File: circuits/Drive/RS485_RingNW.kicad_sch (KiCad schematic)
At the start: 30 parts, among them J13 Conn_01x06_MountingPin, J8 Conn_01x06_MountingPin, Q17 S8550, Q5 S8550, U11 MAX3485, U12 MAX3485, U14 MAX3485, U16 MAX3485

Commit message: 更新
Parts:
- J13, J8: footprint Connector_Molex:Molex_PicoBlade_53261-0671_1x06-1MP_P1.25mm_Horizontal -> Connector_Molex:Molex_PicoBlade_53398-0671_1x06-1MP_P1.25mm_Vertical
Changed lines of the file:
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@@
       (effects (font (size 1.27 1.27)) (justify left))
     )
-    (property "Footprint" "Connector_Molex:Molex_PicoBlade_53261-0671_1x06-1MP_P1.25mm_Horizontal" (at 142.24 86.36 0)
+    (property "Footprint" "Connector_Molex:Molex_PicoBlade_53398-0671_1x06-1MP_P1.25mm_Vertical" (at 142.24 86.36 0)
       (effects (font (size 1.27 1.27)) hide)
     )
@@
       (effects (font (size 1.27 1.27)) (justify left))
     )
-    (property "Footprint" "Connector_Molex:Molex_PicoBlade_53261-0671_1x06-1MP_P1.25mm_Horizontal" (at 276.86 86.36 0)
-      (effects (font (size 1.27 1.27)) hide)
-    )
+    (property "Footprint" "Connector_Molex:Molex_PicoBlade_53398-0671_1x06-1MP_P1.25mm_Vertical" (at 276.86 86.36 0)
+      (effects (font (size 1.27 1.27)) hide)
+    )

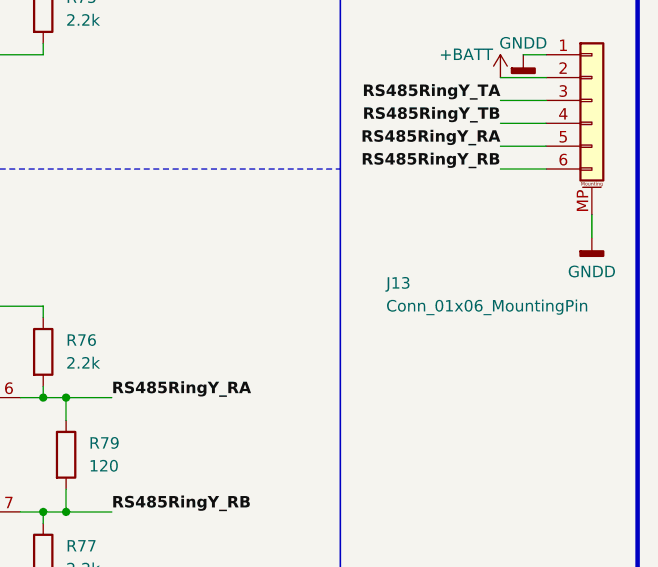
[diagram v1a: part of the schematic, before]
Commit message: 発注_第一弾
Drive, 1stLayer_Power, 2ndLayer_3rdLayer
を発注
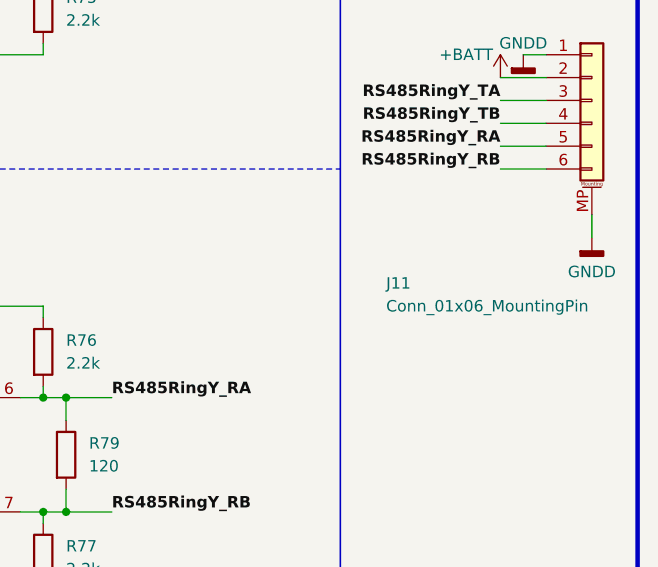
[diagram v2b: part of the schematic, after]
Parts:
- renumbered J13 to J11
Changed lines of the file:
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@@
   (symbol (lib_id "Connector_Generic_MountingPin:Conn_01x06_MountingPin") (at 276.86 86.36 0) (unit 1)
     (in_bom yes) (on_board yes) (dnp no)
-    (property "Reference" "J13" (at 254 106.68 0)
+    (property "Reference" "J11" (at 254 106.68 0)
       (effects (font (size 1.27 1.27)) (justify left))
     )
@@
       (project "Drive"
         (path "/bf4fa0f7-7e40-4646-9c11-e04533c904d6/b3d3e3ee-5cca-468f-bf89-e82456b63441"
-          (reference "J13") (unit 1)
+          (reference "J11") (unit 1)
         )
       )
